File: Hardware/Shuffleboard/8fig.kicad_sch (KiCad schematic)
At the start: 0 parts

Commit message: implemented 7-seg
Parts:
- added C10, C11: 100n, symbol Device:C
- added R15, R16, R17, R18, R19, R20, R21, R22, R23, R24, R25, R26, R27, R28, R29, R30: 100, symbol Device:R
- added U4, U5: INND-TS56RCB, INND-TS56RCB:LED_INND-TS56RCB, symbol INND-TS56RCB:INND-TS56RCB
- added U6, U7: LOGIC-74HC595N_DIP16_, LOGIC-74HC595N_DIP16_:DIP16-2.54-20.32X5.84MM, symbol LOGIC-74HC595N_DIP16_:LOGIC-74HC595N_DIP16_
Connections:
- new net: R29.1, U7.6 (QG)
- new net: R29.2, U5.10
- new net: R23.1, U7.15 (QA)
- new net: R23.2, U5.7
- new net: R16.1, U6.1 (QB)
- new net: R16.2, U4.6
- new net: R21.1, U6.6 (QG)
- new net: R21.2, U4.10
- new net: R18.1, U6.3 (QD)
- new net: R18.2, U4.2
- new net: R17.1, U6.2 (QC)
- new net: R17.2, U4.4
- new net: R15.1, U6.15 (QA)
- new net: R19.1, U6.4 (QE)
- new net: R20.1, U6.5 (QF)
- new net: R22.1, U6.7 (QH)
- new net: U6.9 (QH*), U7.14 (SER)
- new net: R26.1, U7.3 (QD)
- new net: R26.2, U5.2
- new net: R24.1, U7.1 (QB)
- new net: R24.2, U5.6
- new net: R19.2, U4.1
- new net: R22.2, U4.5
- new net: R15.2, U4.7
- new net: R20.2, U4.9
- new net: R27.2, U5.1
- new net: R25.2, U5.4
- new net: R30.2, U5.5
- new net: R28.2, U5.9
- new net: R25.1, U7.2 (QC)
- new net: R27.1, U7.4 (QE)
- new net: R28.1, U7.5 (QF)
- new net: R30.1, U7.7 (QH)
- new net +3.3V: C10.2, C11.2, U6.13 (G), U6.16 (VCC), U7.13 (G), U7.16 (VCC)
- new net GND: C10.1, C11.1, U4.3, U4.8, U5.3, U5.8, U6.10 (SCL), U6.8 (GND), U7.10 (SCL), U7.8 (GND)
- new net PB16_LATCH_PULSE: U6.12 (RCK), U7.12 (RCK)
- new net PB8_MOSI(PICO): U6.14 (SER)
- new net PB9_SPI_CLK: U6.11 (SCK), U7.11 (SCK)
- no-connect marks 0 -> 1
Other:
- note added: "Shift Registers & 7 Segment Displays"

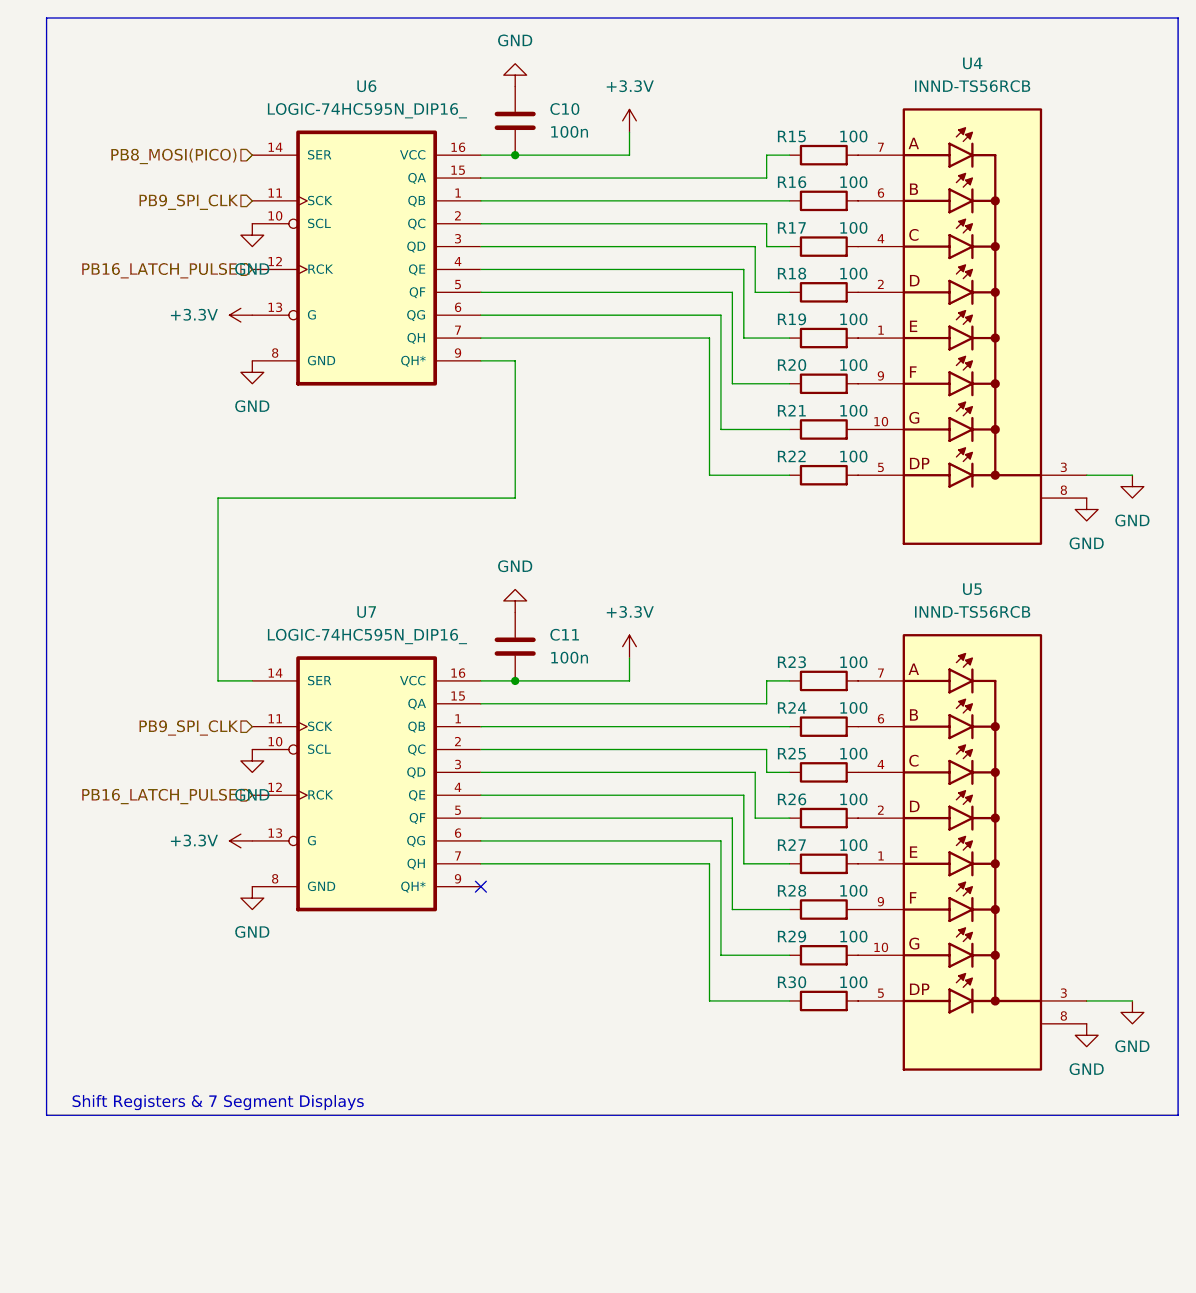
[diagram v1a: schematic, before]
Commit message: footprints, tracing
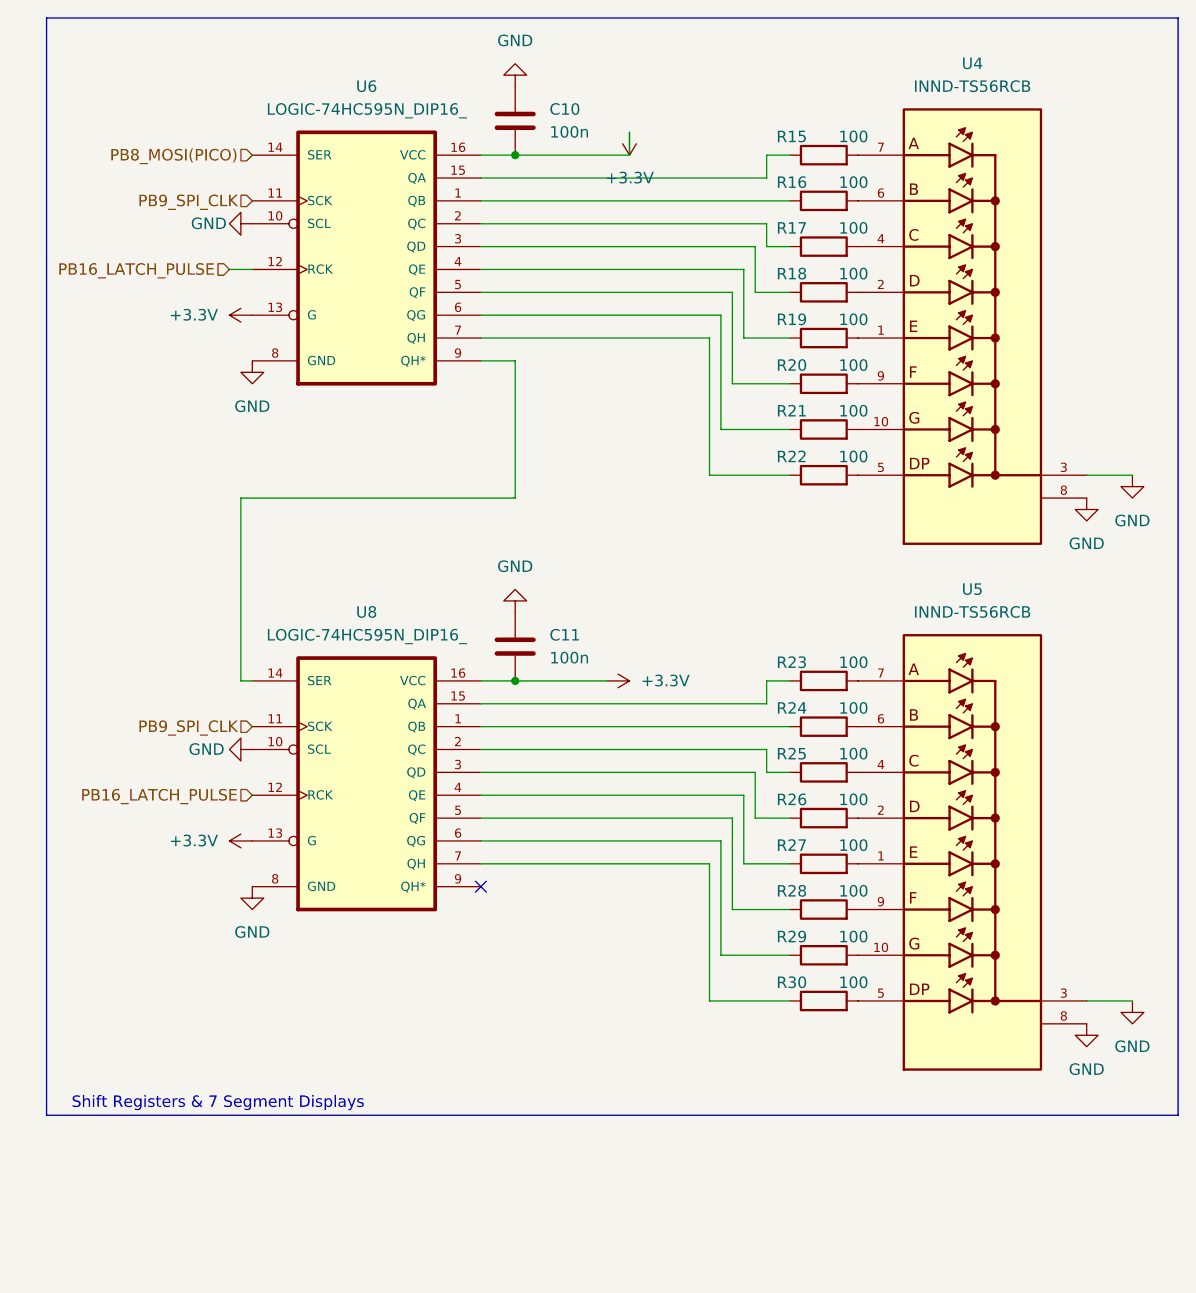
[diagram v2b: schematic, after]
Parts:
- removed U6, U7: LOGIC-74HC595N_DIP16_, LOGIC-74HC595N_DIP16_:DIP16-2.54-20.32X5.84MM, symbol LOGIC-74HC595N_DIP16_:LOGIC-74HC595N_DIP16_
- added U6, U8: LOGIC-74HC595N_DIP16_, ShuffleboardFootprints:SOIC127P600X175-16N, symbol ShuffLogic7:LOGIC-74HC595N_DIP16_
- C10, C11: footprint (none) -> Capacitor_SMD:C_0603_1608Metric_Pad1.08x0.95mm_HandSolder; JLCPCB # (none) -> C1880996; Mouser Link (none) -> https://www.mouser.com/ProductDetail/KYOCERA-AVX/06031C104K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; Mouser Part Number (none) -> 581-06031C104K4T2A
- R15, R16, R17, R18, R19, R20, R21, R22, R23, R24, R25, R26, R27, R28, R29, R30: footprint (none) -> Resistor_SMD:R_0603_1608Metric_Pad0.98x0.95mm_HandSolder; Mouser Link (none) -> https://www.mouser.com/ProductDetail/Vishay/CRCW0603100RJNE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; Mouser Part Number (none) -> 71-CRCW0603100RJNEBC
- U4, U5: footprint INND-TS56RCB:LED_INND-TS56RCB -> ShuffleboardFootprints:LED_INND-TS56RCB; Mouser Link (none) -> https://www.mouser.com/ProductDetail/Inolux/INND-TS56RCB?qs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; Mouser Part Number (none) -> 743-INND-TS56RCB
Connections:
- net +3.3V: now also U6.13 (G), U6.16 (VCC), U8.13 (G), U8.16 (VCC)
- net GND: now also U6.10 (SCL), U6.8 (GND), U8.10 (SCL), U8.8 (GND)
- net PB16_LATCH_PULSE: now also U6.12 (RCK), U8.12 (RCK)
- net PB8_MOSI(PICO): now also U6.14 (SER)
- net PB9_SPI_CLK: now also U6.11 (SCK), U8.11 (SCK)
- net at R29.1: now also U8.6 (QG)
- net at R23.1: now also U8.15 (QA)
- net at R16.1: now also U6.1 (QB)
- net at R21.1: now also U6.6 (QG)
- net at R18.1: now also U6.3 (QD)
- net at R17.1: now also U6.2 (QC)
- net at R15.1: now also U6.15 (QA)
- net at R19.1: now also U6.4 (QE)
- net at R20.1: now also U6.5 (QF)
- net at R22.1: now also U6.7 (QH)
- net at R26.1: now also U8.3 (QD)
- net at R24.1: now also U8.1 (QB)
- net at R25.1: now also U8.2 (QC)
- net at R27.1: now also U8.4 (QE)
- net at R28.1: now also U8.5 (QF)
- net at R30.1: now also U8.7 (QH)
- new net: U6.9 (QH*), U8.14 (SER)

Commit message: layout
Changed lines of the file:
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@@
-	(wire
-		(pts
-			(xy 77.47 27.94) (xy 77.47 25.4)
-		)
-		(stroke
-			(width 0)
-			(type default)
-		)
-	)
 	(wire
 		(pts
@@
 	(symbol
 		(lib_id "power:+3.3V")
-		(at 77.47 25.4 180)
+		(at 77.47 27.94 0)
 		(unit 1)
 		(exclude_from_sim no)
@@
 		(fields_autoplaced yes)
 		(property "Reference" "#PWR049"
-			(at 77.47 21.59 0)
+			(at 77.47 31.75 0)
 			(effects
 				(font
@@
 		)
 		(property "Value" "+3.3V"
-			(at 77.47 30.48 0)
+			(at 77.47 22.86 0)
 			(effects
 				(font
@@
 		)
 		(property "Footprint" ""
-			(at 77.47 25.4 0)
+			(at 77.47 27.94 0)
 			(effects
 				(font
@@
 		)
 		(property "Datasheet" ""
-			(at 77.47 25.4 0)
+			(at 77.47 27.94 0)
 			(effects
 				(font
@@
 		)
 		(property "Description" "Power symbol creates a global label with name \"+3.3V\""
-			(at 77.47 25.4 0)
-			(effects
-				(font
+			(at 77.47 27.94 0)
+			(effects
+				(font

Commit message: layout 2
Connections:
- net QH1: now reaches U6.9 (QH*), U8.14 (SER)
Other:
- moved on the sheet: C11, R23, R24, R25, R26, R27, R28, R29, R30, U5, U8

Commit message: finished layout
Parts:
- C10, C11: value 100n -> (none)
- R15, R16, R17, R18, R19, R20, R21, R22, R23, R24, R25, R26, R27, R28, R29, R30: value 100 -> (none)
- U4, U5: value INND-TS56RCB -> (none)
- U6, U8: value LOGIC-74HC595N_DIP16_ -> (none); VALUE 74HC595N-DIP16 -> (none)

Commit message: finalized
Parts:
- C11: value (none) -> 100n
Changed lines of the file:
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@@
 		(in_pos_files yes)
 		(dnp no)
-		(fields_autoplaced yes)
 		(property "Reference" "C11"
 			(at 68.58 101.5999 0)
@@
 			)
 		)
-		(property "Value" ""
-			(at 64.77 102.87 0)
-			(hide yes)
+		(property "Value" "100n"
+			(at 70.866 103.886 0)
 			(show_name no)
 			(do_not_autoplace no)

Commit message: tht resistors
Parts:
- C10: value (none) -> 100n
- R15, R16, R17, R18, R19, R20, R21, R22, R23, R24, R25, R26, R27, R28, R29, R30: value (none) -> 100

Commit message: updated to end
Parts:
- C10, C11: value 100n -> (none)
- R15, R16, R17, R18, R19, R20, R21, R22, R23, R24, R25, R26, R27, R28, R29, R30: value 100 -> (none)
